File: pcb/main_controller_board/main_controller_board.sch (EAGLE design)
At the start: 3 parts, among them U1 RPI_CAMERA, U2 RPI_CAMERA

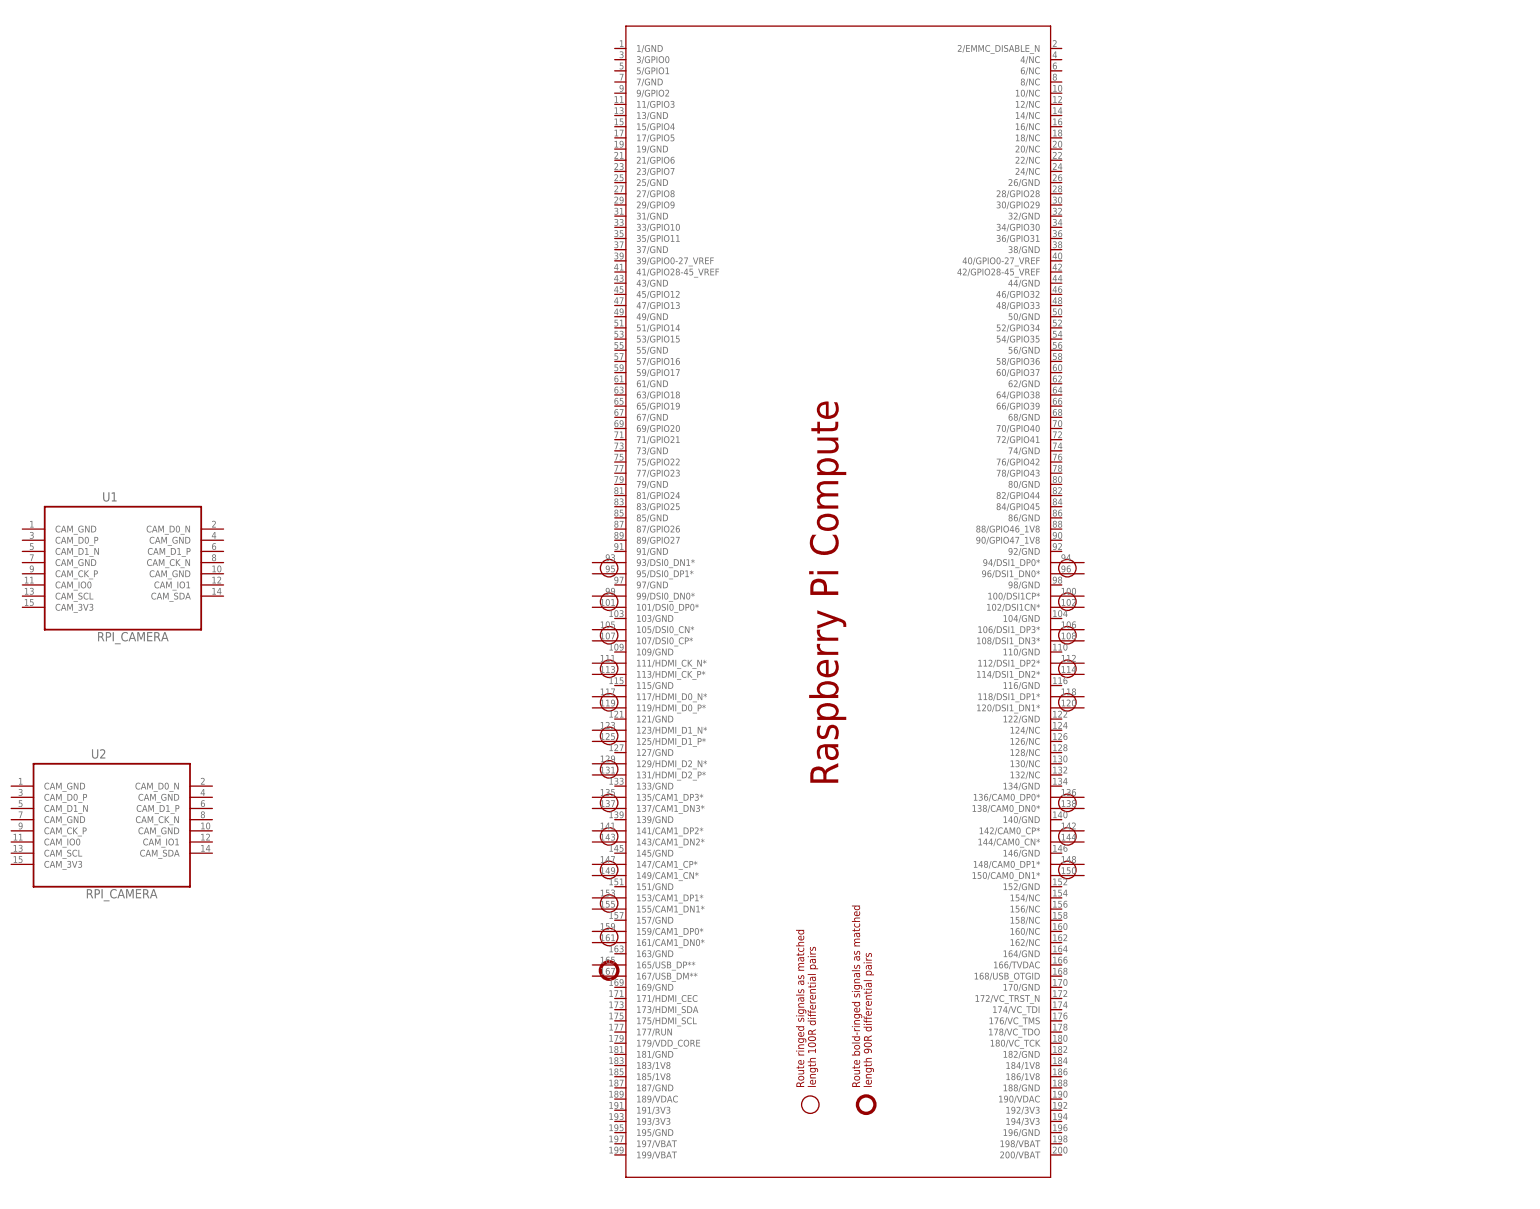
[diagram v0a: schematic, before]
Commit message: add dc-dc
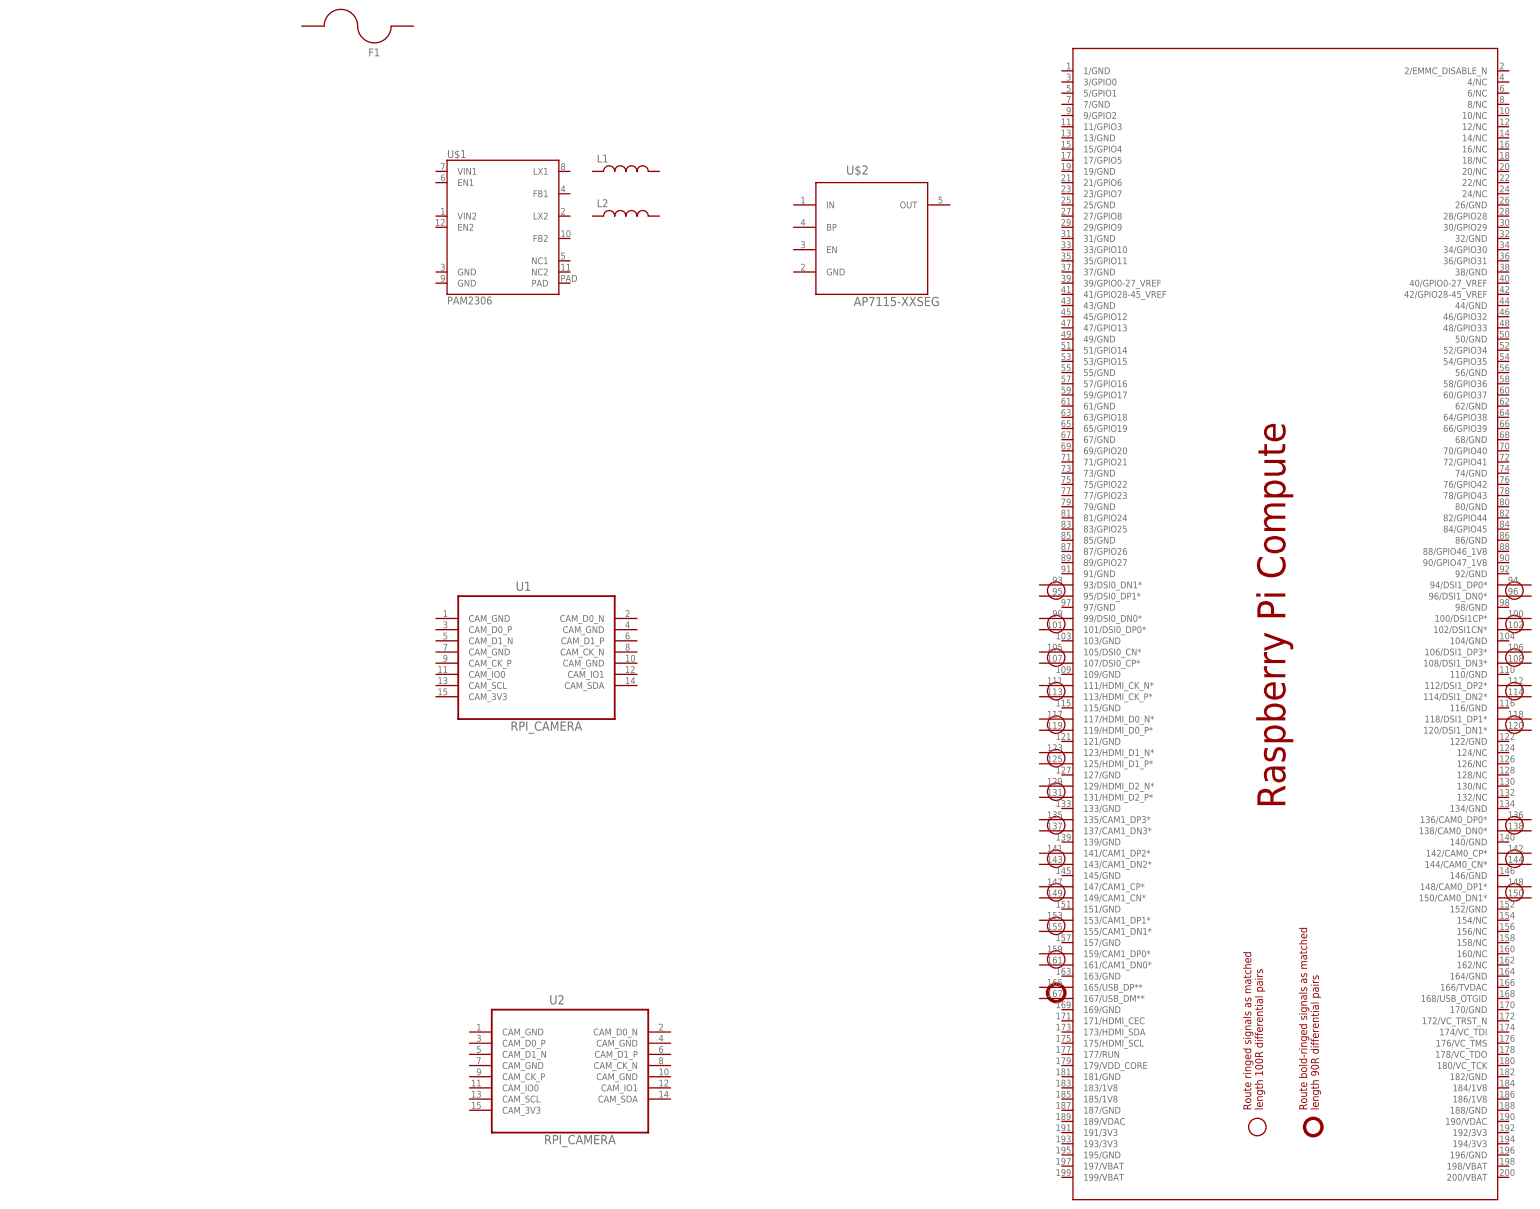
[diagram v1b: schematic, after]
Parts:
- added F1: (no value), openblw:MF-MSMF075/24
- added L1, L2: (no value), openblw:BOURNS-SRN4018
- added U$1: PAM2306, openblw:PAM2306
- added U$2: AP7115-XXSEG, openblw:AP7115-XXSEG
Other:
- moved on the sheet: U1, U2
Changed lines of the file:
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@@
 <layer number="48" name="Document" color="7" fill="1" visible="no" active="no"/>
 <layer number="49" name="Reference" color="7" fill="1" visible="no" active="no"/>
+<layer number="50" name="dxf" color="7" fill="1" visible="no" active="no"/>
 <layer number="51" name="tDocu" color="7" fill="1" visible="no" active="no"/>
 <layer number="52" name="bDocu" color="7" fill="1" visible="no" active="no"/>
+<layer number="53" name="tGND_GNDA" color="7" fill="1" visible="no" active="no"/>
+<layer number="54" name="bGND_GNDA" color="7" fill="1" visible="no" active="no"/>
+<layer number="56" name="wert" color="7" fill="1" visible="no" active="no"/>
+<layer number="57" name="tCAD" color="7" fill="1" visible="no" active="no"/>
+<layer number="59" name="tCarbon" color="7" fill="1" visible="no" active="no"/>
+<layer number="60" name="bCarbon" color="7" fill="1" visible="no" active="no"/>
 <layer number="90" name="Modules" color="5" fill="1" visible="yes" active="yes"/>
 <layer number="91" name="Nets" color="2" fill="1" visible="yes" active="yes"/>
@@
 <layer number="97" name="Info" color="7" fill="1" visible="yes" active="yes"/>
 <layer number="98" name="Guide" color="6" fill="1" visible="yes" active="yes"/>
+<layer number="99" name="SpiceOrder" color="7" fill="1" visible="yes" active="yes"/>
+<layer number="100" name="Mechanical" color="7" fill="1" visible="yes" active="yes"/>
+<layer number="101" name="Gehäuse" color="7" fill="1" visible="yes" active="yes"/>
+<layer number="102" name="ID" color="7" fill="1" visible="yes" active="yes"/>
+<layer number="103" name="tMap" color="7" fill="1" visible="yes" active="yes"/>
+<layer number="104" name="bMap" color="7" fill="1" visible="yes" active="yes"/>
+<layer number="105" name="tPlate" color="7" fill="1" visible="yes" active="yes"/>
+<layer number="106" name="bPlate" color="7" fill="1" visible="yes" active="yes"/>
+<layer number="107" name="Crop" color="7" fill="1" visible="yes" active="yes"/>
+<layer number="108" name="tplace-old" color="10" fill="1" visible="yes" active="yes"/>
+<layer number="109" name="ref-old" color="11" fill="1" visible="yes" active="yes"/>
+<layer number="110" name="fp0" color="7" fill="1" visible="yes" active="yes"/>
+<layer number="111" name="tGTest" color="7" fill="1" visible="yes" active="yes"/>
+<layer number="112" name="bGTest" color="7" fill="1" visible="yes" active="yes"/>
+<layer number="113" name="IDFDebug" color="4" fill="1" visible="yes" active="yes"/>
+<layer number="116" name="Patch_BOT" color="7" fill="1" visible="yes" active="yes"/>
+<layer number="118" name="Rect_Pads" color="7" fill="1" visible="yes" active="yes"/>
+<layer number="121" name="_tsilk" color="7" fill="1" visible="yes" active="yes"/>
+<layer number="122" name="_bsilk" color="7" fill="1" visible="yes" active="yes"/>
+<layer number="123" name="tTestmark" color="7" fill="1" visible="yes" active="yes"/>
+<layer number="124" name="bTestmark" color="7" fill="1" visible="yes" active="yes"/>
+<layer number="125" name="_tNames" color="7" fill="1" visible="yes" active="yes"/>
+<layer number="126" name="_bNames" color="7" fill="1" visible="yes" active="yes"/>
+<layer number="127" name="_tValues" color="7" fill="1" visible="yes" active="yes"/>
+<layer number="128" name="_bValues" color="7" fill="1" visible="yes" active="yes"/>
+<layer number="129" name="Mask" color="7" fill="1" visible="yes" active="yes"/>
+<layer number="131" name="tAdjust" color="7" fill="1" visible="yes" active="yes"/>
+<layer number="132" name="bAdjust" color="7" fill="1" visible="yes" active="yes"/>
+<layer number="144" name="Drill_legend" color="7" fill="1" visible="yes" active="yes"/>
+<layer number="150" name="Notes" color="7" fill="1" visible="yes" active="yes"/>
+<layer number="151" name="HeatSink" color="7" fill="1" visible="yes" active="yes"/>
+<layer number="152" name="_bDocu" color="7" fill="1" visible="yes" active="yes"/>
+<layer number="153" name="FabDoc1" color="7" fill="1" visible="yes" active="yes"/>
+<layer number="154" name="FabDoc2" color="7" fill="1" visible="yes" active="yes"/>
+<layer number="155" name="FabDoc3" color="7" fill="1" visible="yes" active="yes"/>
+<layer number="199" name="EXTD_ERC" color="7" fill="1" visible="yes" active="yes"/>
 <layer number="200" name="200bmp" color="1" fill="10" visible="yes" active="yes"/>
 <layer number="201" name="201bmp" color="2" fill="10" visible="no" active="yes"/>
+<layer number="202" name="202bmp" color="3" fill="10" visible="yes" active="yes"/>
+<layer number="203" name="203bmp" color="4" fill="10" visible="yes" active="yes"/>
+<layer number="204" name="204bmp" color="5" fill="10" visible="yes" active="yes"/>
+<layer number="205" name="205bmp" color="6" fill="10" visible="yes" active="yes"/>
+<layer number="206" name="206bmp" color="7" fill="10" visible="yes" active="yes"/>
+<layer number="207" name="207bmp" color="8" fill="10" visible="yes" active="yes"/>
+<layer number="208" name="208bmp" color="9" fill="10" visible="yes" active="yes"/>
+<layer number="209" name="209bmp" color="7" fill="1" visible="yes" active="yes"/>
+<layer number="210" name="210bmp" color="7" fill="1" visible="yes" active="yes"/>
+<layer number="211" name="211bmp" color="7" fill="1" visible="yes" active="yes"/>
+<layer number="212" name="212bmp" color="7" fill="1" visible="yes" active="yes"/>
+<layer number="213" name="213bmp" color="7" fill="1" visible="yes" active="yes"/>
+<layer number="214" name="214bmp" color="7" fill="1" visible="yes" active="yes"/>
+<layer number="215" name="215bmp" color="7" fill="1" visible="yes" active="yes"/>
+<layer number="216" name="216bmp" color="7" fill="1" visible="yes" active="yes"/>
+<layer number="217" name="217bmp" color="18" fill="1" visible="no" active="no"/>
+<layer number="218" name="218bmp" color="19" fill="1" visible="no" active="no"/>
+<layer number="219" name="219bmp" color="20" fill="1" visible="no" active="no"/>
+<layer number="220" name="220bmp" color="21" fill="1" visible="no" active="no"/>
+<layer number="221" name="221bmp" color="22" fill="1" visible="no" active="no"/>
+<layer number="222" name="222bmp" color="23" fill="1" visible="no" active="no"/>
+<layer number="223" name="223bmp" color="24" fill="1" visible="no" active="no"/>
+<layer number="224" name="224bmp" color="25" fill="1" visible="no" active="no"/>
+<layer number="225" name="225bmp" color="7" fill="1" visible="yes" active="yes"/>
+<layer number="226" name="226bmp" color="7" fill="1" visible="yes" active="yes"/>
+<layer number="227" name="227bmp" color="7" fill="1" visible="yes" active="yes"/>
+<layer number="228" name="228bmp" color="7" fill="1" visible="yes" active="yes"/>
+<layer number="229" name="229bmp" color="7" fill="1" visible="yes" active="yes"/>
+<layer number="230" name="230bmp" color="7" fill="1" visible="yes" active="yes"/>
+<layer number="231" name="231bmp" color="7" fill="1" visible="yes" active="yes"/>
+<layer number="248" name="Housing" color="7" fill="1" visible="yes" active="yes"/>
+<layer number="249" name="Edge" color="7" fill="1" visible="yes" active="yes"/>
+<layer number="250" name="Descript" color="3" fill="1" visible="no" active="no"/>
+<layer number="251" name="SMDround" color="7" fill="1" visible="yes" active="yes"/>
+<layer number="254" name="cooling" color="7" fill="1" visible="yes" active="yes"/>
+<layer number="255" name="routoute" color="7" fill="1" visible="yes" active="yes"/>
 </layers>
 <schematic xreflabel="%F%N/%S.%C%R" xrefpart="/%S.%C%R">
@@
 <part name="U1" library="openblw" deviceset="RPI_CAMERA" device=""/>
 <part name="U2" library="openblw" deviceset="RPI_CAMERA" device=""/>
+<part name="U$1" library="openblw" deviceset="PAM2306" device=""/>
+<part name="U$2" library="openblw" deviceset="AP7115-XX" device="SEG"/>
+<part name="L1" library="openblw" deviceset="BOURNS-SRN4018" device=""/>
+<part name="L2" library="openblw" deviceset="BOURNS-SRN4018" device=""/>
+<part name="F1" library="openblw" deviceset="MF-MSMF*?" device="" technology="075/24"/>
 </parts>
 <sheets>
@@
 </plain>
 <instances>
-<instance part="PCB1" gate="G$1" x="144.78" y="160.02"/>
-<instance part="U1" gate="A" x="-17.78" y="162.56"/>
-<instance part="U2" gate="A" x="-20.32" y="104.14"/>
+<instance part="PCB1" gate="G$1" x="246.38" y="154.94"/>
+<instance part="U1" gate="A" x="76.2" y="142.24"/>
+<instance part="U2" gate="A" x="83.82" y="48.26"/>
+<instance part="U$1" gate="G$1" x="68.58" y="231.14"/>
+<instance part="U$2" gate="G$1" x="134.62" y="241.3"/>
+<instance part="L1" gate="G$1" x="96.52" y="248.92"/>
+<instance part="L2" gate="G$1" x="96.52" y="238.76"/>
+<instance part="F1" gate="G$1" x="35.56" y="281.94" rot="R90"/>
 </instances>
 <busses>

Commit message: porovisional wiring
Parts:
- added C1, C9: 100n, resistor:C-EUC0402
- added C10: 4.7u, resistor:C-EUC0603
- added C11, C12, C13, C14: (no value), resistor:C-EUC1206
- added C2, C3, C6, C7: 10u, resistor:C-EUC0805
- added C4, C5: NF, resistor:C-EUC0402
- added C8: 1u, resistor:C-EUC0402
- added CN1: (no value), openblw:JST_2PIN-THM
- added H1, H2, H3, H4: MOUNT-PAD-ROUND2.8, holes:MOUNT-PAD-ROUND2.8
- added IC1: (no value), openblw:VR_1OUTXX
- added JP1: (no value), pinhead:PINHD-1X4
- added K1: 61400416021, openblw:61400416021
- added LED1: RED, led:LEDCHIP-LED0603
- added LED2: GREEN, led:LEDCHIP-LED0603
- added R1, R11, R12: 100K, resistor:R-EU_R0402
- added R10, R7, R8, R9: 0R, resistor:R-EU_R0805
- added R13, R14, R16, R17: 1.8K, resistor:R-EU_R0402
- added R15, R6: 470R, resistor:R-EU_R0402
- added R2, R3: 0R, resistor:R-EU_R0402
- added R4, R5: NR, resistor:R-EU_R0402
- added U$3: DMG1012T, openblw:DMG1012T
- F1: value (none) -> MF-MSMF110/16
- L1, L2: value (none) -> 4.7u
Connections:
- new net +12V: F1.2, IC1.IN
- new net +1V8: C5.1, C7.1, L2.1, R3.1, R9.2
- new net +2V5: C10.1, R10.2, U$2.OUT@5
- new net +3V3: C4.1, C6.1, C8.1, L1.1, R13.2, R14.2, R15.1, R16.2, R17.2, R2.1, R6.1, R7.2, R8.2, U$2.EN@3, U$2.IN@1, U1.CAM_3V3@15, U2.CAM_3V3@15
- new net +5V: C11.1, C2.1, C3.1, IC1.OUT, JP1.1, K1.VCC, R1.1, U$1.EN1@6, U$1.VIN1@7, U$1.VIN2@1
- new net BOTTOM_LIGHT_ENABLED: PCB1.59/GPIO17
- new net CAM0_CN: PCB1.144/CAM0_CN*, U1.CAM_CK_N@8
- new net CAM0_CP: PCB1.142/CAM0_CP*, U1.CAM_CK_P@9
- new net CAM0_DN0: PCB1.138/CAM0_DN0*, U1.CAM_D0_N@2
- new net CAM0_DN1: PCB1.150/CAM0_DN1*, U1.CAM_D1_N@5
- new net CAM0_DP0: PCB1.136/CAM0_DP0*, U1.CAM_D0_P@3
- new net CAM0_DP1: PCB1.148/CAM0_DP1*, U1.CAM_D1_P@6
- new net CAM0_IO0: PCB1.36/GPIO31, U1.CAM_IO0@11
- new net CAM0_IO1: PCB1.34/GPIO30, U1.CAM_IO1@12
- new net CAM0_SCL: PCB1.30/GPIO29, R13.1, U1.CAM_SCL@13
- new net CAM0_SDA: PCB1.28/GPIO28, R14.1, U1.CAM_SDA@14
- new net CAM1_CN: PCB1.149/CAM1_CN*, U2.CAM_CK_N@8
- new net CAM1_CP: PCB1.147/CAM1_CP*, U2.CAM_CK_P@9
- new net CAM1_DN0: PCB1.161/CAM1_DN0*, U2.CAM_D0_N@2
- new net CAM1_DN1: PCB1.155/CAM1_DN1*, U2.CAM_D1_N@5
- new net CAM1_DP0: PCB1.159/CAM1_DP0*, U2.CAM_D0_P@3
- new net CAM1_DP1: PCB1.153/CAM1_DP1*, U2.CAM_D1_P@6
- new net CAM1_IO0: PCB1.11/GPIO3, U2.CAM_IO0@11
- new net CAM1_IO1: PCB1.9/GPIO2, U2.CAM_IO1@12
- new net CAM1_SCL: PCB1.5/GPIO1, R17.1, U2.CAM_SCL@13
- new net CAM1_SDA: PCB1.3/GPIO0, R16.1, U2.CAM_SDA@14
- new net CM_1V8: C12.1, PCB1.183/1V8, PCB1.184/1V8, PCB1.185/1V8, PCB1.186/1V8, R9.1
- new net CM_3V3: C13.1, PCB1.191/3V3, PCB1.192/3V3, PCB1.193/3V3, PCB1.194/3V3, R8.1
- new net CM_VBAT: C14.1, PCB1.197/VBAT, PCB1.198/VBAT, PCB1.199/VBAT, PCB1.200/VBAT, R7.1
- new net CM_VDAC: PCB1.189/VDAC, PCB1.190/VDAC, R10.1
- new net EMMC_DISABLE_N: PCB1.2/EMMC_DISABLE_N
- new net EXT0: PCB1.63/GPIO18
- new net EXT1: PCB1.65/GPIO19
- new net GND: C1.2, C10.2, C11.2, C12.2, C13.2, C14.2, C2.2, C3.2, C6.2, C7.2, C8.2, C9.2, CN1.1, H1.MOUNT, H2.MOUNT, H3.MOUNT, H4.MOUNT, IC1.GND, JP1.4, K1.GND, LED1.C, PCB1.1/GND, PCB1.103/GND, PCB1.104/GND, PCB1.109/GND, PCB1.110/GND, PCB1.115/GND, PCB1.121/GND, PCB1.122/GND, PCB1.127/GND, PCB1.13/GND, PCB1.133/GND, PCB1.134/GND, PCB1.139/GND, PCB1.140/GND, PCB1.145/GND, PCB1.146/GND, PCB1.151/GND, PCB1.152/GND, PCB1.157/GND, PCB1.163/GND, PCB1.164/GND, PCB1.169/GND, PCB1.170/GND, PCB1.181/GND, PCB1.182/GND, PCB1.187/GND, PCB1.188/GND, PCB1.19/GND, PCB1.195/GND, PCB1.196/GND, PCB1.25/GND, PCB1.26/GND, PCB1.31/GND, PCB1.32/GND, PCB1.37/GND, PCB1.38/GND, PCB1.43/GND, PCB1.44/GND, PCB1.49/GND, PCB1.50/GND, PCB1.55/GND, PCB1.56/GND, PCB1.61/GND, PCB1.62/GND, PCB1.67/GND, PCB1.68/GND, PCB1.7/GND, PCB1.73/GND, PCB1.74/GND, PCB1.79/GND, PCB1.80/GND, PCB1.85/GND, PCB1.86/GND, PCB1.91/GND, PCB1.92/GND, PCB1.97/GND, PCB1.98/GND, R11.2, R12.2, R4.2, R5.2, U$1.GND@3, U$1.GND@9, U$1.PAD, U$2.GND@2, U$3.S, U1.CAM_GND@1, U1.CAM_GND@10, U1.CAM_GND@4, U1.CAM_GND@7, U2.CAM_GND@1, U2.CAM_GND@10, U2.CAM_GND@4, U2.CAM_GND@7
- new net GPIO47_1V8: PCB1.90/GPIO47_1V8, U$3.G
- new net N$1: C1.1, R1.2, U$1.EN2@12
- new net N$10: C5.2, R3.2, R4.1, U$1.FB2@10
- new net N$11: PCB1.154/NC
- new net N$12: PCB1.156/NC
- new net N$13: PCB1.158/NC
- new net N$14: PCB1.160/NC
- new net N$15: PCB1.162/NC
- new net N$16: PCB1.10/NC
- new net N$17: PCB1.12/NC
- new net N$18: PCB1.14/NC
- new net N$19: PCB1.16/NC
- new net N$2: L1.2, U$1.LX1@8
- new net N$20: PCB1.18/NC
- new net N$21: PCB1.20/NC
- new net N$22: PCB1.22/NC
- new net N$23: PCB1.24/NC
- new net N$24: PCB1.124/NC
- new net N$25: PCB1.126/NC
- new net N$26: PCB1.128/NC
- new net N$27: PCB1.130/NC
- new net N$28: PCB1.132/NC
- new net N$29: PCB1.4/NC
- new net N$3: U$1.NC1@5
- new net N$30: PCB1.6/NC
- new net N$31: PCB1.82/GPIO44, R12.1
- new net N$32: LED2.A, R15.2
- new net N$33: LED2.C, U$3.D
- new net N$34: PCB1.84/GPIO45, R11.1
- new net N$35: PCB1.8/NC
- new net N$4: U$1.NC2@11
- new net N$5: C9.1, U$2.BP@4
- new net N$6: CN1.2, F1.1
- new net N$7: L2.2, U$1.LX2@2
- new net N$8: C4.2, R2.2, R5.1, U$1.FB1@4
- new net N$9: LED1.A, R6.2
- new net TOP_LIGHT_ENABLED: PCB1.57/GPIO16
- new net UART_RX: JP1.3, PCB1.53/GPIO15
- new net UART_TX: JP1.2, PCB1.51/GPIO14
- new net USB_DN: K1.D-, PCB1.167/USB_DM**
- new net USB_DP: K1.D+, PCB1.165/USB_DP**
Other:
- note added: "Camera"
- note added: "Interfaces"
- note added: "Power"
- note added: "RPCM"
- moved on the sheet: F1, L1, L2, U$1, U$2, U1, U2

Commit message: rev0.1
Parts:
- added U$4: TENDA_P200, openblw:TENDA_P200
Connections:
- net CAM0_CN renamed CAM0_C_N
- net CAM0_CP renamed CAM0_C_P
- net CAM0_DN0 renamed CAM0_D0_N
- net CAM0_DN1 renamed CAM0_D1_N
- net CAM0_DP0 renamed CAM0_D0_P
- net CAM0_DP1 renamed CAM0_D1_P
- net CAM1_CN renamed CAM1_C_N
- net CAM1_CP renamed CAM1_C_P
- net CAM1_DN0 renamed CAM1_D0_N
- net CAM1_DN1 renamed CAM1_D1_N
- net CAM1_DP0 renamed CAM1_D0_P
- net CAM1_DP1 renamed CAM1_D1_P
- net USB_DN renamed USB_D_N
- net USB_DP renamed USB_D_P
- new net DGND: U$4.INN
- net +12V: now also U$4.INP
- net +3V3: now also U$4.3V3
- net GND: now also U$4.GND
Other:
- note added: "Hole"

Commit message: before export gerber
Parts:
- added C15: 10u, resistor:C-EUC1206
- C11: value (none) -> 22u
- PCB1: value RPI_COMPUTE -> RPCM
- U1: value RPI_CAMERA -> CAMERA0
- U2: value RPI_CAMERA -> CAMERA1
- renumbered U$1 to U5, U$2 to U6, U$3 to U3, U$4 to U4
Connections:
- net DGND renamed PLC_N
- new net PLC_P: U4.INP
- net +12V: now also C15.1; no longer U4.INP
- net GND: now also C15.2
